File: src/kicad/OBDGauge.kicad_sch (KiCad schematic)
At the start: 19 parts, among them J1 OBD, J2 Neopixel, J3 TM1637, J4 9V REG, Q1 3906, SW1 SW1, SW2 SW2, U1 LM2903

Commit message: Add files via upload
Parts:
- added R8: 10K, Resistor_THT:R_Axial_DIN0204_L3.6mm_D1.6mm_P7.62mm_Horizontal, symbol Device:R
- R5: value 30K -> 47K
- R6: value 15K -> 10K
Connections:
- net 12V: now also R8.1
- net K+: now also R8.2
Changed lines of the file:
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@@
+	)
+	(junction
+		(at 106.68 88.9)
+		(diameter 0)
+		(color 0 0 0 0)
 	)
 	(junction
@@
 	(wire
 		(pts
+			(xy 106.68 88.9) (xy 106.68 104.14)
+		)
+		(stroke
+			(width 0)
+			(type default)
+		)
+	)
+	(wire
+		(pts
 			(xy 147.32 83.82) (xy 179.07 83.82)
 		)
@@
 	(wire
 		(pts
-			(xy 106.68 69.85) (xy 106.68 104.14)
+			(xy 106.68 69.85) (xy 106.68 88.9)
 		)
 		(stroke
@@
 	(wire
 		(pts
+			(xy 101.6 88.9) (xy 106.68 88.9)
+		)
+		(stroke
+			(width 0)
+			(type default)
+		)
+	)
+	(wire
+		(pts
 			(xy 96.52 53.34) (xy 96.52 77.47)
 		)
@@
 		(pts
 			(xy 130.686 50.3414) (xy 130.686 48.26)
+		)
+		(stroke
+			(width 0)
+			(type default)
+		)
+	)
+	(wire
+		(pts
+			(xy 96.52 96.52) (xy 101.6 96.52)
 		)
 		(stroke
@@
 			)
 			(justify left bottom)
+		)
+	)
+	(symbol
+		(lib_id "Device:R")
+		(at 101.6 92.71 180)
+		(unit 1)
+		(exclude_from_sim no)
+		(in_bom yes)
+		(on_board yes)
+		(dnp no)
+		(property "Reference" "R8"
+			(at 100.33 85.344 0)
+			(effects
+				(font
+					(size 1.27 1.27)
+				)
+				(justify right)
+			)
+		)
+		(property "Value" "10K"
+			(at 99.822 87.376 0)
+			(effects
+				(font
+					(size 1.27 1.27)
+				)
+				(justify right)
+			)
+		)
+		(property "Footprint" "Resistor_THT:R_Axial_DIN0204_L3.6mm_D1.6mm_P7.62mm_Horizontal"
+			(at 103.378 92.71 90)
+			(effects
+				(font
+					(size 1.27 1.27)
+				)
+				(hide yes)
+			)
+		)
+		(property "Datasheet" "~"
+			(at 101.6 92.71 0)
+			(effects
+				(font
+					(size 1.27 1.27)
+				)
+				(hide yes)
+			)
+		)
+		(property "Description" ""
+			(at 101.6 92.71 0)
+			(effects
+				(font
+					(size 1.27 1.27)
+				)
+				(hide yes)
+			)
+		)
+		(pin "1"
+		)
+		(pin "2"
+		)
+		(instances
+			(project "OBDGauge"
+				(path "/c695e2af-e235-4bd5-bb08-67902a8024a4"
+					(reference "R8")
+					(unit 1)
+				)
+			)
 		)
 	)
@@
 			)
 		)
-		(property "Value" "15K"
+		(property "Value" "10K"
 			(at 149.86 137.1601 0)
 			(effects
@@
 			)
 		)
-		(property "Value" "30K"
+		(property "Value" "47K"
 			(at 149.86 129.5399 0)
 			(effects

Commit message: Add files via upload
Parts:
- R8: value 10K -> 510
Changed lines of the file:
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@@
 			)
 		)
-		(property "Value" "10K"
+		(property "Value" "510"
 			(at 99.822 87.376 0)
 			(effects

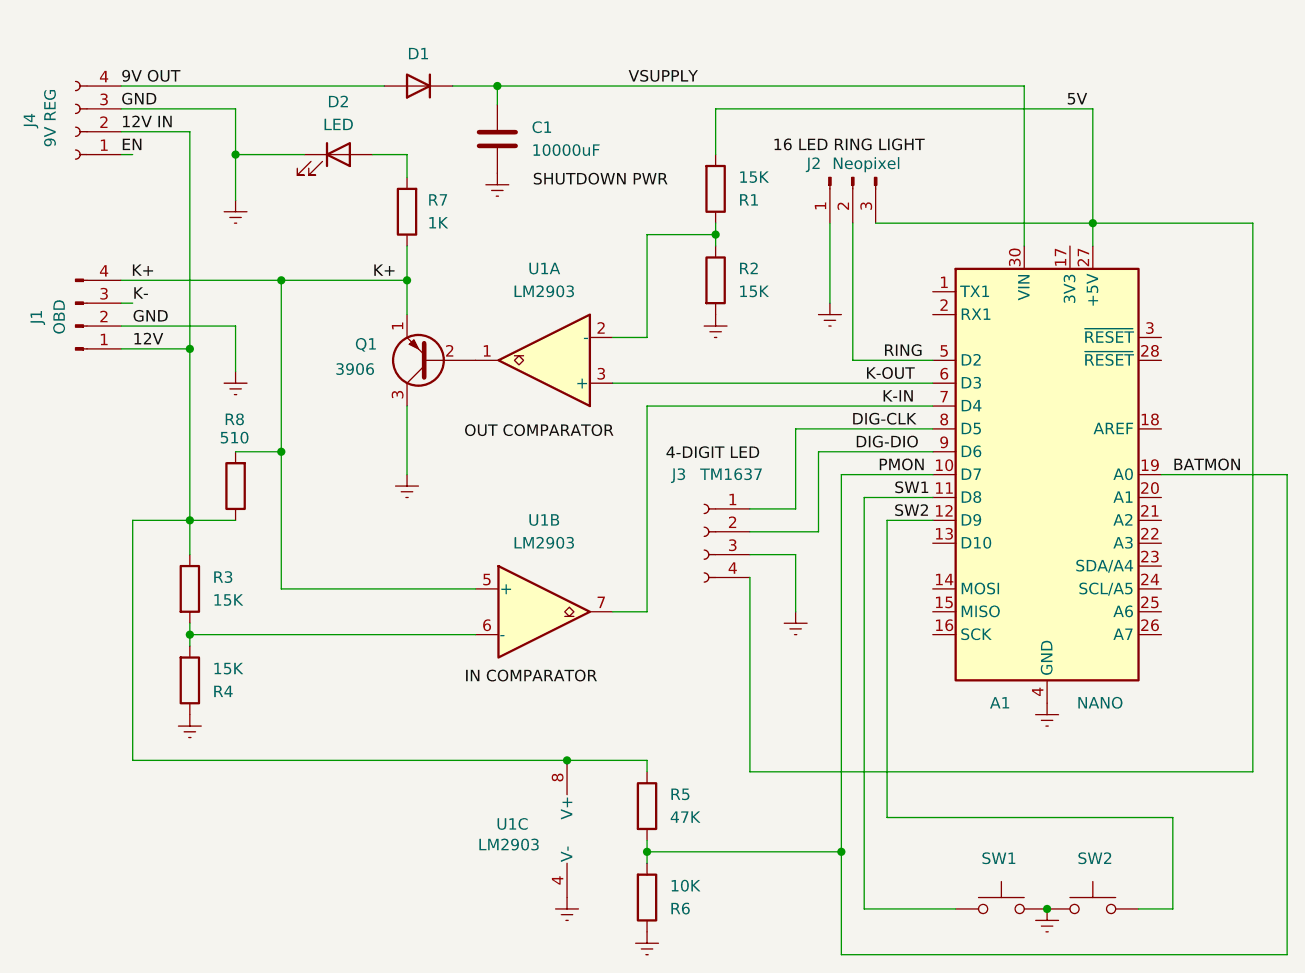
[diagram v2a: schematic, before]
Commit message: Updated to reflect Nano Every
Updated voltage divider value and note to reflect voltage regulator no longer needed for Nano Every.
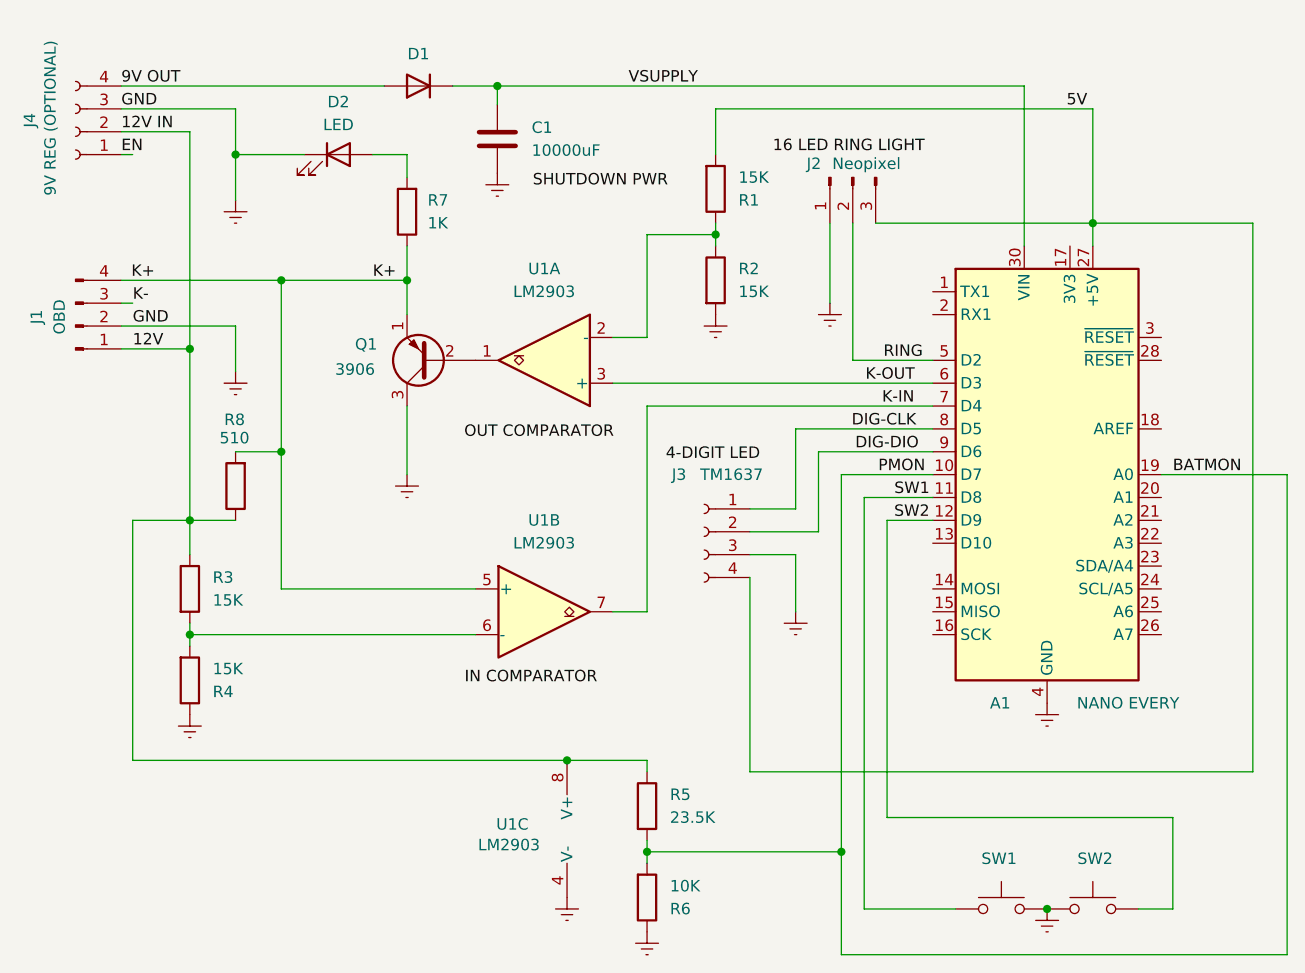
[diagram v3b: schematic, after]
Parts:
- A1: value NANO -> NANO EVERY
- J4: value 9V REG -> 9V REG (OPTIONAL)
- R5: value 47K -> 23.5K
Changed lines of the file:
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@@
 			)
 		)
-		(property "Value" "NANO"
+		(property "Value" "NANO EVERY"
 			(at 195.072 116.84 0)
 			(effects
@@
 			)
 		)
-		(property "Value" "9V REG"
+		(property "Value" "9V REG (OPTIONAL)"
 			(at 81.026 51.816 90)
 			(effects
@@
 			)
 		)
-		(property "Value" "47K"
+		(property "Value" "23.5K"
 			(at 149.86 129.5399 0)
 			(effects
